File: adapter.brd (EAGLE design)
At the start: 57.1 x 35.6 mm, 5 parts, among them U1 DS12885, X1 32.768kHz

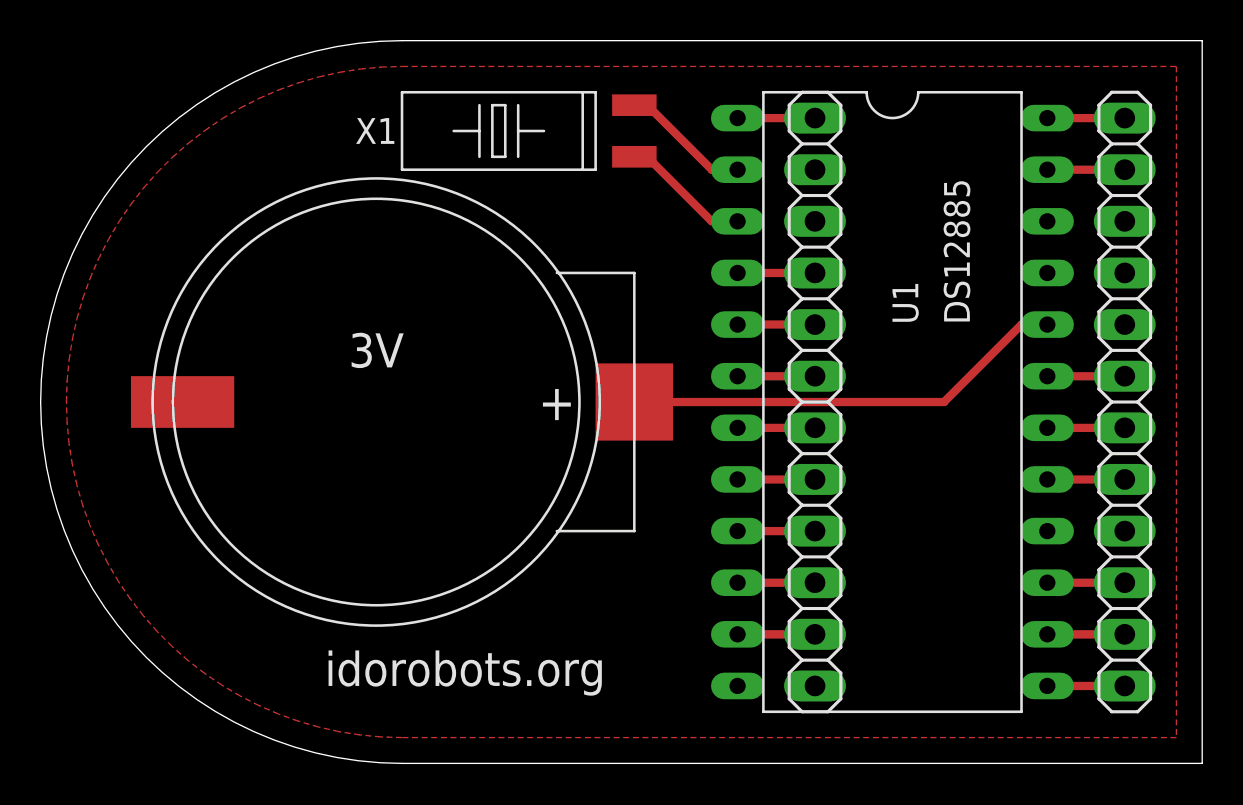
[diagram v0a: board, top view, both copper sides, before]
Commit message: Made PCB border smaller.
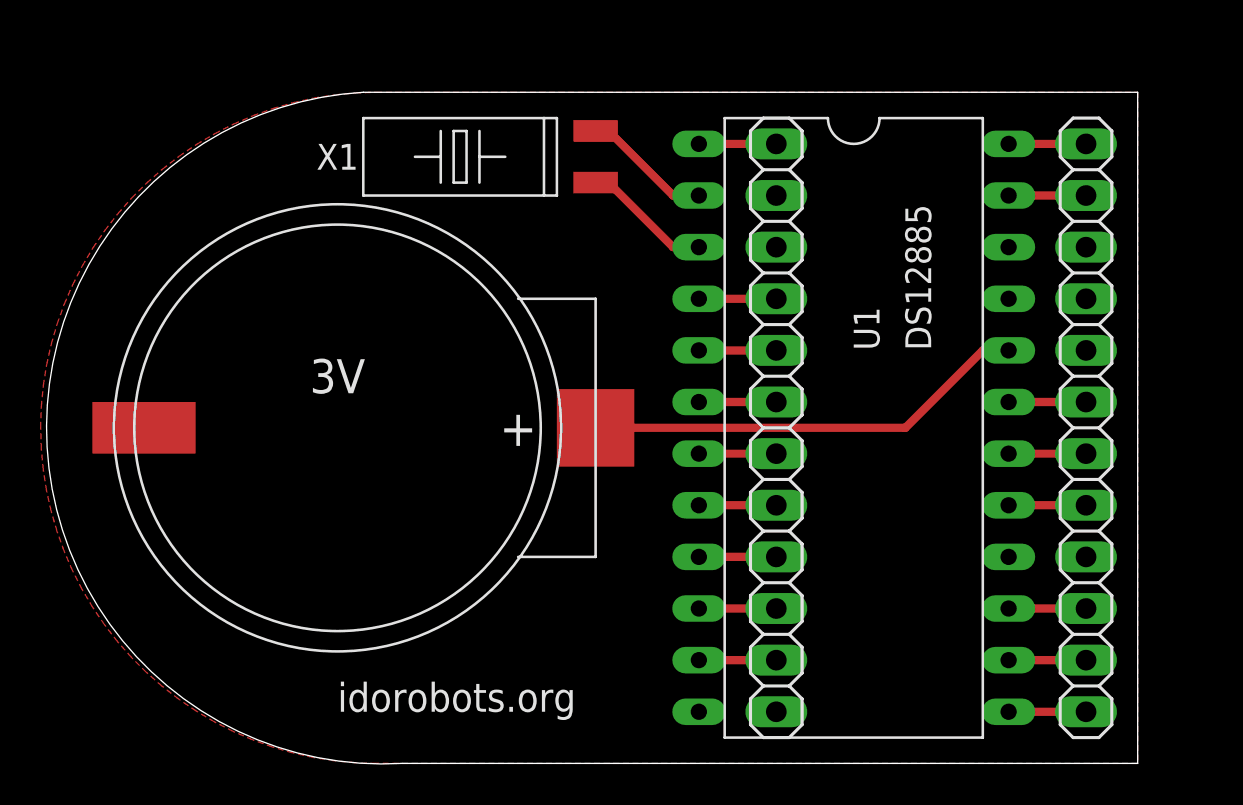
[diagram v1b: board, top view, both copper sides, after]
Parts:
- moved 3V 2.29 mm to (14.6, 16.5)
- moved JP1 2.29 mm to (36.2, 16.5)
- moved JP2 2.29 mm to (51.4, 16.5)
- moved X1 2.29 mm to (26.0, 29.8)
- moved U1 2.29 mm to (40.0, 16.5)
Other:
- board size 57.1 x 35.6 mm -> 53.7 x 33 mm
